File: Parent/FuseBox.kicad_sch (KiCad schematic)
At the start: 25 parts, among them J1 Screw Terminal, J10 Screw Terminal, J11 Screw Terminal, J12 Screw Terminal, J13 Screw Terminal, J2 Screw Terminal, J3 Screw Terminal, J4 Screw Terminal, J5 Screw Terminal, J6 Screw Terminal, J7 Screw Terminal, J8 Screw Terminal, J9 Screw Terminal

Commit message: Worked on Parent - Move Workspace to cloud
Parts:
- added D9: D, symbol Device:D
- added F1: Battery Charger Fuse, symbol Device:Fuse
- added J1: Screw Terminal, symbol Connector:Screw_Terminal_01x01
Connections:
- net Battery Terminal +: now also D9.1 (K)
- new net: D9.2 (A), F1.1
- new net Battery Charger : F1.2, J1.1 (Pin_1)

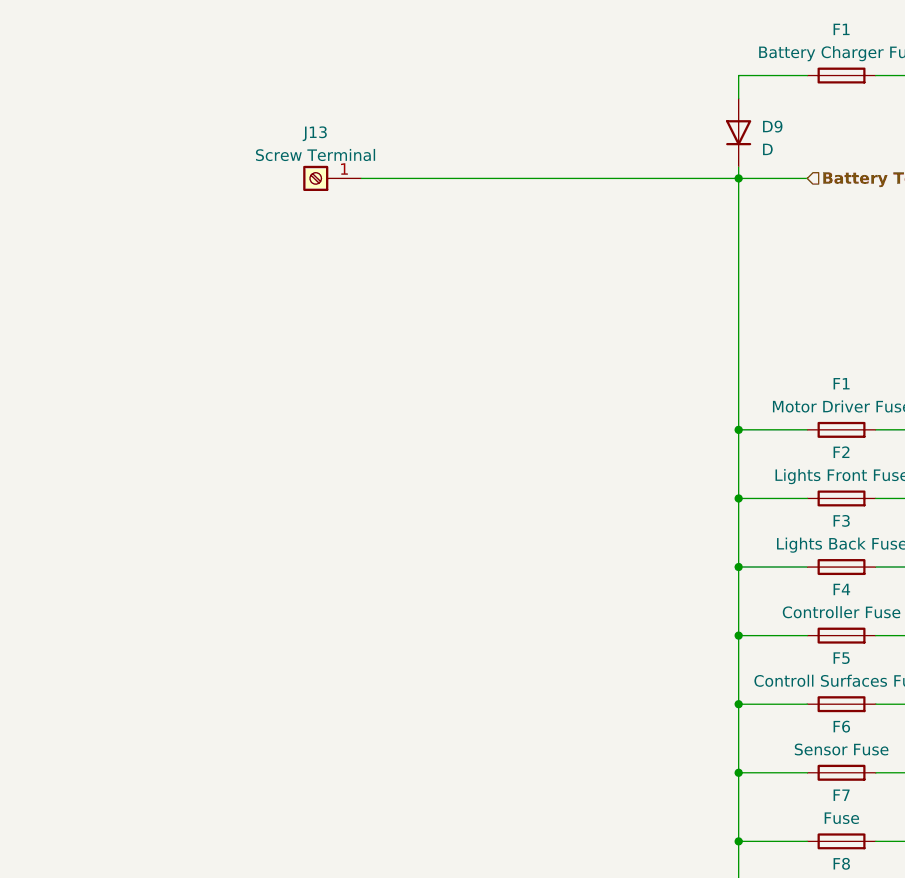
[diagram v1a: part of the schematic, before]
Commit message: Updated Parent further - Move workspace to cloud
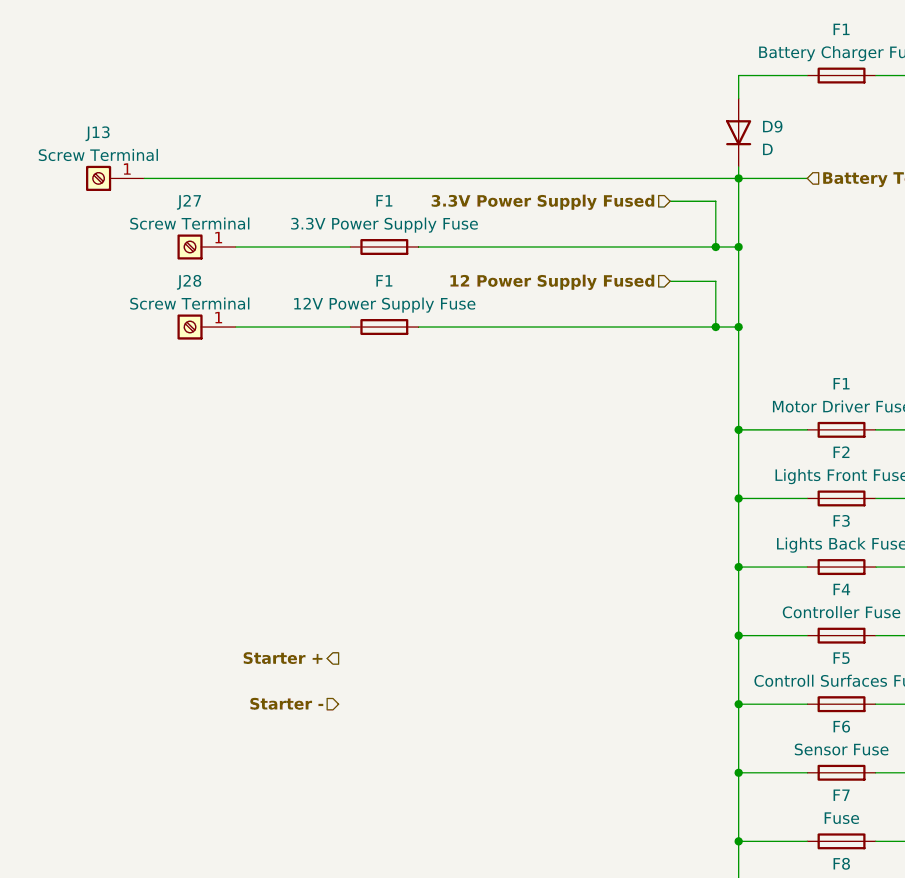
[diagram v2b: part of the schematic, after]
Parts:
- added F1: 3.3V Power Supply Fuse, symbol Device:Fuse
- added F1: 12V Power Supply Fuse, symbol Device:Fuse
- added J27, J28: Screw Terminal, symbol Connector:Screw_Terminal_01x01
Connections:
- net Battery Terminal + renamed 12 Power Supply Fused
- net 12 Power Supply Fused: now also F1.2, F1.2
- new net: F1.1, J27.1 (Pin_1)
- new net: F1.1, J28.1 (Pin_1)
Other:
- moved on the sheet: J13
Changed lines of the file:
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@@
   (junction (at 96.52 99.06) (diameter 0) (color 0 0 0 0)
   )
+  (junction (at 93.98 48.26) (diameter 0) (color 0 0 0 0)
+  )
   (junction (at 96.52 40.64) (diameter 0) (color 0 0 0 0)
   )
+  (junction (at 96.52 48.26) (diameter 0) (color 0 0 0 0)
+  )
   (junction (at 96.52 76.2) (diameter 0) (color 0 0 0 0)
   )
@@
   (junction (at 96.52 91.44) (diameter 0) (color 0 0 0 0)
   )
+  (junction (at 93.98 57.15) (diameter 0) (color 0 0 0 0)
+  )
   (junction (at 121.92 68.58) (diameter 0) (color 0 0 0 0)
   )
@@
   (junction (at 96.52 121.92) (diameter 0) (color 0 0 0 0)
   )
+  (junction (at 96.52 57.15) (diameter 0) (color 0 0 0 0)
+  )
   (junction (at 121.92 91.44) (diameter 0) (color 0 0 0 0)
   )
@@
   (junction (at 121.92 99.06) (diameter 0) (color 0 0 0 0)
   )
+  (wire (pts (xy 93.98 43.18) (xy 93.98 48.26))
+    (stroke (width 0) (type default))
+  )
   (wire (pts (xy 96.52 129.54) (xy 104.14 129.54))
     (stroke (width 0) (type default))
@@
     (stroke (width 0) (type default))
   )
+  (wire (pts (xy 96.52 57.15) (xy 96.52 68.58))
+    (stroke (width 0) (type default))
+  )
   (wire (pts (xy 96.52 106.68) (xy 104.14 106.68))
     (stroke (width 0) (type default))
@@
     (stroke (width 0) (type default))
   )
+  (wire (pts (xy 60.96 48.26) (xy 93.98 48.26))
+    (stroke (width 0) (type default))
+  )
   (wire (pts (xy 121.92 87.63) (xy 121.92 91.44))
     (stroke (width 0) (type default))
   )
+  (wire (pts (xy 93.98 57.15) (xy 96.52 57.15))
+    (stroke (width 0) (type default))
+  )
   (wire (pts (xy 96.52 91.44) (xy 96.52 99.06))
     (stroke (width 0) (type default))
@@
     (stroke (width 0) (type default))
   )
-  (wire (pts (xy 54.61 40.64) (xy 96.52 40.64))
+  (wire (pts (xy 30.48 40.64) (xy 96.52 40.64))
     (stroke (width 0) (type default))
   )
@@
     (stroke (width 0) (type default))
   )
+  (wire (pts (xy 88.9 52.07) (xy 93.98 52.07))
+    (stroke (width 0) (type default))
+  )
   (wire (pts (xy 121.92 83.82) (xy 153.67 83.82))
     (stroke (width 0) (type default))
@@
     (stroke (width 0) (type default))
   )
+  (wire (pts (xy 93.98 48.26) (xy 96.52 48.26))
+    (stroke (width 0) (type default))
+  )
+  (wire (pts (xy 96.52 48.26) (xy 96.52 57.15))
+    (stroke (width 0) (type default))
+  )
   (wire (pts (xy 96.52 29.21) (xy 104.14 29.21))
     (stroke (width 0) (type default))
@@
     (stroke (width 0) (type default))
   )
+  (wire (pts (xy 60.96 57.15) (xy 93.98 57.15))
+    (stroke (width 0) (type default))
+  )
+  (wire (pts (xy 88.9 43.18) (xy 93.98 43.18))
+    (stroke (width 0) (type default))
+  )
   (wire (pts (xy 96.52 76.2) (xy 96.52 83.82))
     (stroke (width 0) (type default))
@@
     (stroke (width 0) (type default))
   )
+  (wire (pts (xy 93.98 52.07) (xy 93.98 57.15))
+    (stroke (width 0) (type default))
+  )
   (wire (pts (xy 111.76 83.82) (xy 121.92 83.82))
     (stroke (width 0) (type default))
@@
     (stroke (width 0) (type default))
   )
+  (wire (pts (xy 40.64 48.26) (xy 53.34 48.26))
+    (stroke (width 0) (type default))
+  )
   (wire (pts (xy 96.52 76.2) (xy 104.14 76.2))
     (stroke (width 0) (type default))
@@
     (stroke (width 0) (type default))
   )
-  (wire (pts (xy 96.52 40.64) (xy 96.52 68.58))
+  (wire (pts (xy 40.64 57.15) (xy 53.34 57.15))
+    (stroke (width 0) (type default))
+  )
+  (wire (pts (xy 96.52 40.64) (xy 96.52 48.26))
     (stroke (width 0) (type default))
   )
@@
     (effects (font (size 1.27 1.27) bold) (justify left))
   )
+  (hierarchical_label "Starter -" (shape input) (at 52.07 99.06 180) (fields_autoplaced)
+    (effects (font (size 1.27 1.27) bold) (justify right))
+  )
+  (hierarchical_label "3.3V Power Supply Fused" (shape input) (at 88.9 43.18 180) (fields_autoplaced)
+    (effects (font (size 1.27 1.27) bold) (justify right))
+  )
+  (hierarchical_label "Starter +" (shape output) (at 52.07 93.98 180) (fields_autoplaced)
+    (effects (font (size 1.27 1.27) bold) (justify right))
+  )
   (hierarchical_label "Motor Driver Fused" (shape input) (at 124.46 64.77 0) (fields_autoplaced)
     (effects (font (size 1.27 1.27) bold) (justify left))
@@
     (effects (font (size 1.27 1.27) bold) (justify left))
   )
+  (hierarchical_label "12 Power Supply Fused" (shape input) (at 88.9 52.07 180) (fields_autoplaced)
+    (effects (font (size 1.27 1.27) bold) (justify right))
+  )
   (hierarchical_label "Battery Charger " (shape input) (at 124.46 25.4 0) (fields_autoplaced)
     (effects (font (size 1.27 1.27) bold) (justify left))
@@
     )
   )
-  (symbol (lib_id "Connector:Screw_Terminal_01x01") (at 49.53 40.64 180) (unit 1)
-    (in_bom yes) (on_board yes) (dnp no) (fields_autoplaced)
-    (property "Reference" "J13" (at 49.53 35.56 0)
-      (effects (font (size 1.27 1.27)))
-    )
-    (property "Value" "Screw Terminal" (at 49.53 38.1 0)
-      (effects (font (size 1.27 1.27)))
-    )
-    (property "Footprint" "" (at 49.53 40.64 0)
-      (effects (font (size 1.27 1.27)) hide)
-    )
-    (property "Datasheet" "~" (at 49.53 40.64 0)
+  (symbol (lib_id "Connector:Screw_Terminal_01x01") (at 25.4 40.64 180) (unit 1)
+    (in_bom yes) (on_board yes) (dnp no) (fields_autoplaced)
+    (property "Reference" "J13" (at 25.4 35.56 0)
+      (effects (font (size 1.27 1.27)))
+    )
+    (property "Value" "Screw Terminal" (at 25.4 38.1 0)
+      (effects (font (size 1.27 1.27)))
+    )
+    (property "Footprint" "" (at 25.4 40.64 0)
+      (effects (font (size 1.27 1.27)) hide)
+    )
+    (property "Datasheet" "~" (at 25.4 40.64 0)
       (effects (font (size 1.27 1.27)) hide)
     )
@@
     )
   )
+  (symbol (lib_id "Device:Fuse") (at 57.15 48.26 90) (unit 1)
+    (in_bom yes) (on_board yes) (dnp no) (fields_autoplaced)
+    (property "Reference" "F1" (at 57.15 43.18 90)
+      (effects (font (size 1.27 1.27)))
+    )
+    (property "Value" "3.3V Power Supply Fuse" (at 57.15 45.72 90)
+      (effects (font (size 1.27 1.27)))
+    )
+    (property "Footprint" "" (at 57.15 50.038 90)
+      (effects (font (size 1.27 1.27)) hide)
+    )
+    (property "Datasheet" "~" (at 57.15 48.26 0)
+      (effects (font (size 1.27 1.27)) hide)
+    )
+    (pin "1")
+    (pin "2")
+    (instances
+      (project "Parent"
+        (path "/1451ec1d-c665-471b-ba41-1d89ef6a63bf"
+          (reference "F1") (unit 1)
+        )
+        (path "/1451ec1d-c665-471b-ba41-1d89ef6a63bf/6dc6ec49-e1c0-477f-a1f4-0d3f7cb3d03c"
+          (reference "F2") (unit 1)
+        )
+      )
+    )
+  )
   (symbol (lib_id "Connector:Screw_Terminal_01x01") (at 158.75 129.54 0) (unit 1)
     (in_bom yes) (on_board yes) (dnp no) (fields_autoplaced)
@@
         )
       )
+    )
+  )
+  (symbol (lib_id "Connector:Screw_Terminal_01x01") (at 35.56 57.15 180) (unit 1)
+    (in_bom yes) (on_board yes) (dnp no) (fields_autoplaced)
+    (property "Reference" "J28" (at 35.56 52.07 0)
+      (effects (font (size 1.27 1.27)))
+    )
+    (property "Value" "Screw Terminal" (at 35.56 54.61 0)
+      (effects (font (size 1.27 1.27)))
+    )
+    (property "Footprint" "" (at 35.56 57.15 0)
+      (effects (font (size 1.27 1.27)) hide)
+    )
+    (property "Datasheet" "~" (at 35.56 57.15 0)
+      (effects (font (size 1.27 1.27)) hide)
+    )
+    (pin "1")
+    (instances
+      (project "Parent"
+        (path "/1451ec1d-c665-471b-ba41-1d89ef6a63bf/6dc6ec49-e1c0-477f-a1f4-0d3f7cb3d03c"
+          (reference "J28") (unit 1)
+        )
+      )
+    )
+  )
+  (symbol (lib_id "Device:Fuse") (at 57.15 57.15 90) (unit 1)
+    (in_bom yes) (on_board yes) (dnp no) (fields_autoplaced)
+    (property "Reference" "F1" (at 57.15 52.07 90)
+      (effects (font (size 1.27 1.27)))
+    )
+    (property "Value" "12V Power Supply Fuse" (at 57.15 54.61 90)
+      (effects (font (size 1.27 1.27)))
+    )
+    (property "Footprint" "" (at 57.15 58.928 90)
+      (effects (font (size 1.27 1.27)) hide)
+    )
+    (property "Datasheet" "~" (at 57.15 57.15 0)
+      (effects (font (size 1.27 1.27)) hide)
+    )
+    (pin "1")
+    (pin "2")
+    (instances
+      (project "Parent"
+        (path "/1451ec1d-c665-471b-ba41-1d89ef6a63bf"
+          (reference "F1") (unit 1)
+        )
+        (path "/1451ec1d-c665-471b-ba41-1d89ef6a63bf/6dc6ec49-e1c0-477f-a1f4-0d3f7cb3d03c"
+          (reference "F4") (unit 1)
+        )
+      )
+    )
+  )
+  (symbol (lib_id "Connector:Screw_Terminal_01x01") (at 35.56 48.26 180) (unit 1)
+    (in_bom yes) (on_board yes) (dnp no) (fields_autoplaced)
+    (property "Reference" "J27" (at 35.56 43.18 0)
+      (effects (font (size 1.27 1.27)))
+    )
+    (property "Value" "Screw Terminal" (at 35.56 45.72 0)
+      (effects (font (size 1.27 1.27)))
+    )
+    (property "Footprint" "" (at 35.56 48.26 0)
+      (effects (font (size 1.27 1.27)) hide)
+    )
+    (property "Datasheet" "~" (at 35.56 48.26 0)
+      (effects (font (size 1.27 1.27)) hide)
+    )
+    (pin "1")
+    (instances
+      (project "Parent"
+        (path "/1451ec1d-c665-471b-ba41-1d89ef6a63bf/6dc6ec49-e1c0-477f-a1f4-0d3f7cb3d03c"
+          (reference "J27") (unit 1)
+        )
+      )

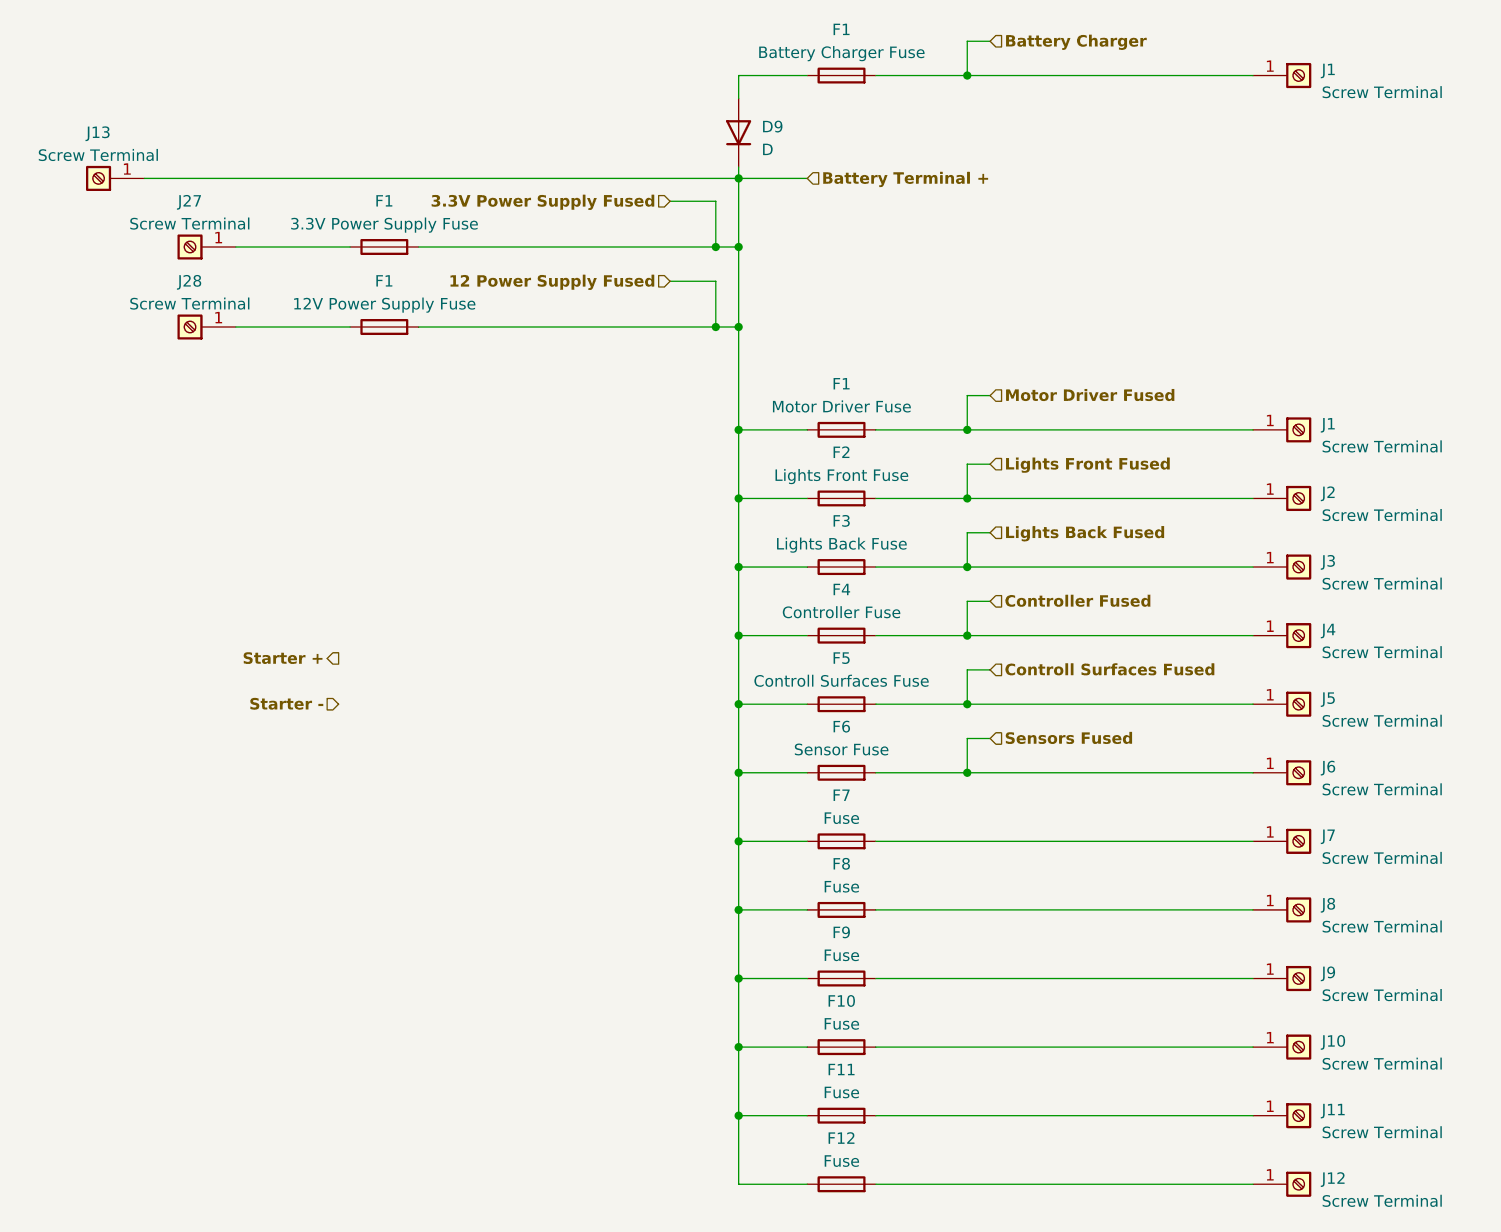
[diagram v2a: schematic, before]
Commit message: Updated Parent - Moved workspace to cloud
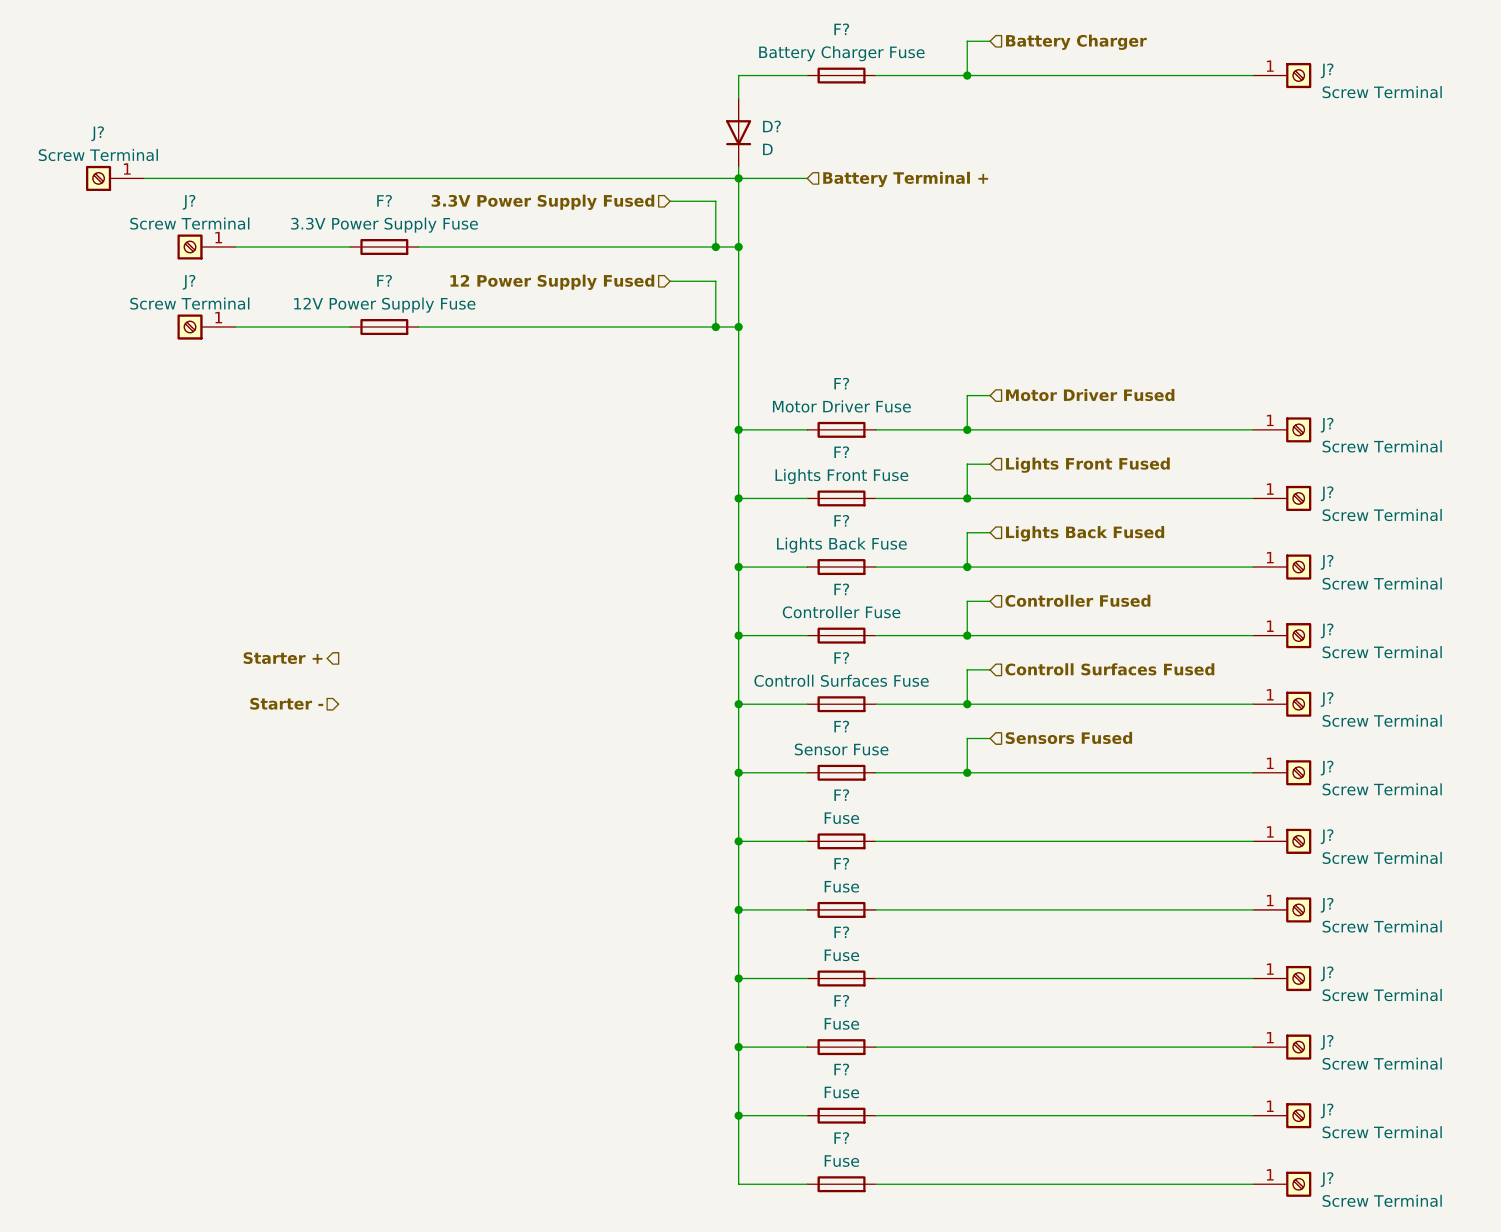
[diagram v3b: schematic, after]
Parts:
- renumbered D9 to D?, F1 to F?, F12 to F?, F9 to F?, F3 to F?, F6 to F?, F5 to F?, F10 to F?, F2 to F?, F11 to F?, F8 to F?, F4 to F?, F7 to F?, J6 to J?, J10 to J?, J7 to J?, J2 to J?, J3 to J?, J5 to J?, J4 to J?, J11 to J?, J13 to J?, J1 to J?, J8 to J?, J9 to J?, J12 to J?, J28 to J?, J27 to J?
